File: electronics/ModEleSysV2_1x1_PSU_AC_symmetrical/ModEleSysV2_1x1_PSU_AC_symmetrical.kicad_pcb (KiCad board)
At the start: 2 copper layers, 43.2 x 49.5 mm, 30 parts, among them J2 Jack-DC, SW1 switch_DPDT, U1 LM317, U2 LM337

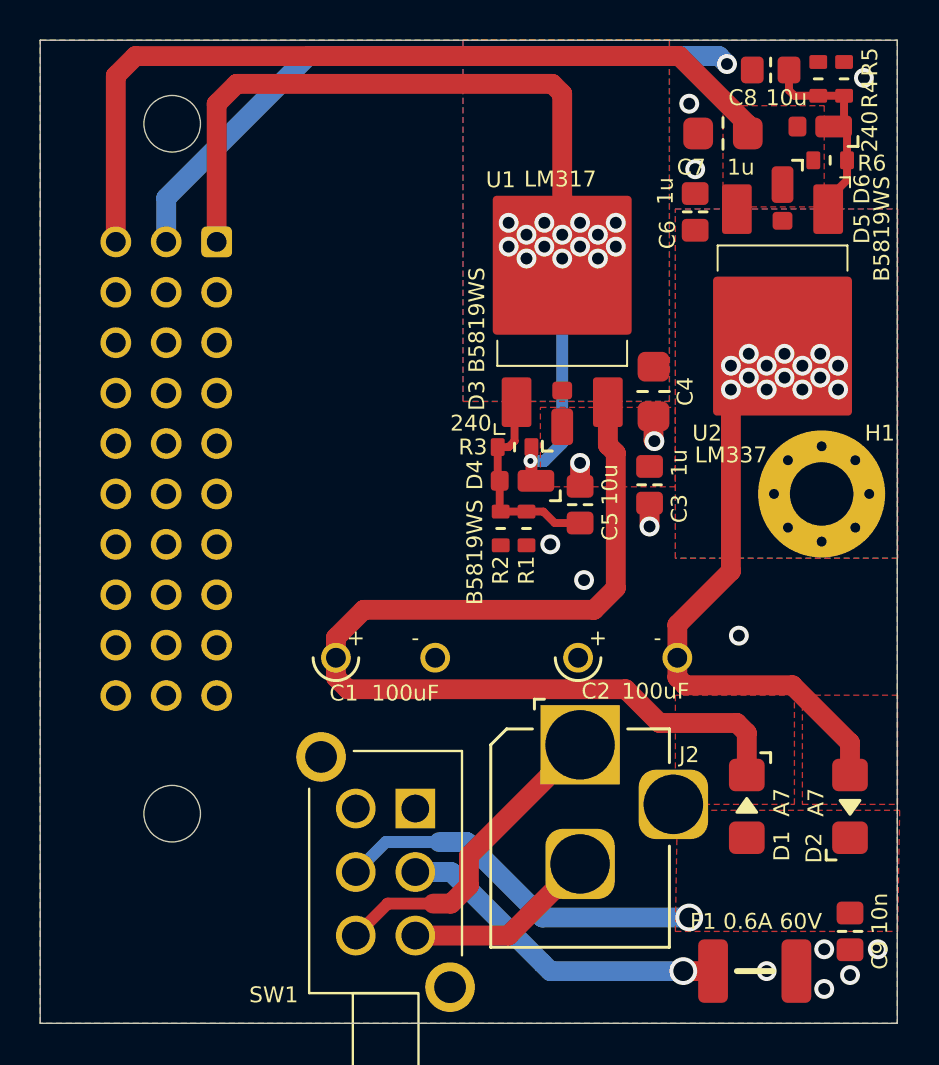
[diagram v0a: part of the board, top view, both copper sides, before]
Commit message: updated PCB with easier to place components and added more output capacitance
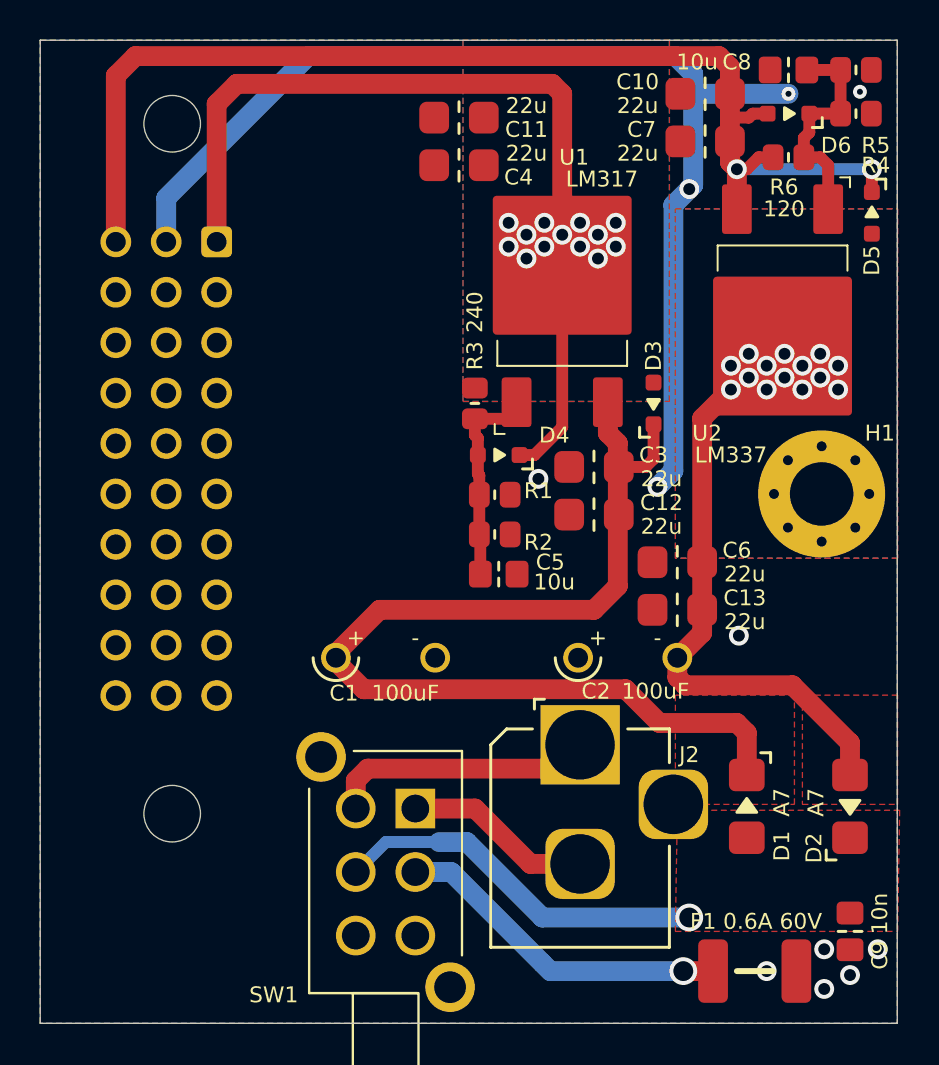
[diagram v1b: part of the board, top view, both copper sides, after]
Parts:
- added C10: 22u, SquantorCapacitor:C_1206_0805, F.Cu at (173.2, 66.2)
- added C11: 22u, SquantorCapacitor:C_1206_0805, F.Cu at (160.8, 67.4)
- added C12: 22u, SquantorCapacitor:C_1206_0805, F.Cu at (167.6, 87.4)
- added C13: 22u, SquantorCapacitor:C_1206_0805, F.Cu at (171.8, 92.2)
- C3, C6: value 1u -> 22u; footprint SquantorCapacitor:C_0805+0603 -> SquantorCapacitor:C_1206_0805
- C4, C7: value 1u -> 22u
- D3, D4, D5, D6: footprint SquantorDiodes:SOD-323HE-shikues -> SquantorDiodes:SOD-323-nexperia-hand
- R1, R2, R3, R4, R5: footprint SquantorResistor:R_0603_hand -> SquantorResistor:R_0805+0603
- R6: value 240 -> 120; footprint SquantorResistor:R_0603_hand -> SquantorResistor:R_0805+0603
- moved C6 17.7 mm to (171.8, 89.8), turned to 180 degrees
- moved C4 15.0 mm to (160.8, 69.8), turned to 180 degrees
- moved C5 5.39 mm to (162.8, 90.4), turned to 0 degrees
- moved D3 4.63 mm to (170.6, 81.8)
- moved D5 4.56 mm to (181.6, 72.2)
- moved R3 2.97 mm to (161.6, 81.8), turned to 90 degrees
- moved C3 2.94 mm to (167.6, 85.0), turned to 180 degrees
- moved R1 2.33 mm to (162.6, 86.4), turned to 0 degrees
- moved R6 2.11 mm to (177.4, 69.4)
- moved R5 1.95 mm to (180.8, 65.0), turned to 0 degrees
- moved R4 1.85 mm to (180.8, 67.2), turned to 0 degrees
- moved D4 1.77 mm to (162.8, 84.4)
- moved D6 1.73 mm to (177.4, 67.2)
- moved C7 0.98 mm to (173.2, 68.6)
- moved C8 0.90 mm to (177.4, 65.0)
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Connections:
- SW1 pad 1: unconnected-(SW1-SW1_P1-Pad1) -> /AC_NEUT_IN
- SW1 pad 3: /AC_NEUT_IN -> unconnected-(SW1-SW1_P2-Pad3)
- SW1 pad 4: /AC_PHASE1_IN -> unconnected-(SW1-SW2_P2-Pad4)
- SW1 pad 6: unconnected-(SW1-SW2_P2-Pad6) -> /AC_PHASE1_IN
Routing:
- net GND: track 37.2 -> 58.4 mm, vias 15 -> 11
- net /-aV: track 42.5 -> 59.3 mm, vias 0 -> 2
- net /DC1p: track 50.6 -> 53.5 mm
- net /AC_PHASE1_IN: track 16.2 -> 13.5 mm
- net /+aV: track 45.2 -> 43.0 mm, vias 15 -> 13
- net /-adj: track 10.3 -> 11.4 mm
- removed copper zone on F.Cu, net /-aV

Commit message: some more PCB modifications, changing output caps to larger values
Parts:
- removed C10, C11, C12, C13: 22u, SquantorCapacitor:C_1206_0805
- C4, C7: footprint SquantorCapacitor:C_1206_0805 -> SquantorCapacitor:C-025-065-elco
- moved C4 2.30 mm to (160.9, 67.5)
- moved C7 1.70 mm to (171.9, 67.5)
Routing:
- net /-aV: track 59.3 -> 60.7 mm
- net GND: track 58.4 -> 57.2 mm
- net /+aV: vias 13 -> 14

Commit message: preparations for production
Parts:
- N1: value 20240426 -> 20250323
- moved C7 0.45 mm to (171.4, 67.4)
- moved C4 0.06 mm to (160.9, 67.4)
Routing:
- net /-aV: track 60.7 -> 61.9 mm
- net /DC1n: track 27.5 -> 28.6 mm
- net /+aV: track 43.0 -> 42.5 mm

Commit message: reviewed and updated PCB's
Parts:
- removed SW1: switch_DPDT, SquantorSwitches:PS-22F02
- added J3: PINS_2X03, SquantorConnectors:DLL-XHY-6A, B.Cu at (47.5, 73.9)
- C1, C2: moved to B.Cu
- C4, C7: value 22u -> 47u
- U1, U2: footprint SquantorIC:TO-252_D-PAK_IRF -> SquantorIC:SOT-223
- moved C6 116.5 mm to (62.3, 49.9)
- moved R3 116.1 mm to (51.7, 44.3)
- moved U2 115.9 mm to (67.4, 41.4)
- moved C5 115.9 mm to (53.1, 52.9)
- moved D4 115.9 mm to (53.1, 46.9)
- moved C3 115.9 mm to (57.9, 47.5)
- moved D3 115.9 mm to (60.9, 44.3)
- moved R1 115.9 mm to (52.9, 48.9)
- moved R2 115.9 mm to (52.9, 50.9)
- moved D5 114.9 mm to (71.9, 38.1)
- moved D1 114.7 mm to (65.6, 68.6)
- moved J1 114.7 mm to (36.4, 51.6)
- moved R4 114.7 mm to (71.1, 33.7)
- moved R5 114.7 mm to (71.1, 31.5)
- moved C8 114.7 mm to (67.7, 31.5)
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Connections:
- J2 pad 1: /AC_PHASE1_IN -> /AC_NEUT_IN
- J2 pad 2: /AC_NEUT_IN -> /AC_PHASE1_IN
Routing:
- net /DC1p: track 53.5 -> 39.2 mm
- net /DC1n: track 28.6 -> 38.6 mm, vias 14 -> 10
- net /+aV: track 42.5 -> 32.5 mm, vias 14 -> 10
- net Net-(F1-Pad1): track 17.1 -> 24.3 mm
- net /AC_PHASE1_IN: track 13.5 -> 8.44 mm
- net /AC1_PHASE: track 19.0 -> 14.0 mm
- net /AC_NEUT_IN: track 9.46 -> 13.5 mm
- net GND: track 56.7 -> 52.8 mm, vias 11 -> 10

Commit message: Updated for production
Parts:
- N1: value 20250323 -> V:20260118
- moved D5 14.1 mm to (61.9, 28.1)
- moved D6 14.1 mm to (57.7, 23.7)
- moved H1 14.1 mm to (59.4, 42.9)
- moved J3 14.1 mm to (37.5, 63.9)
- moved U2 14.1 mm to (57.4, 31.4)
- moved C1 14.1 mm to (40.5, 49.8)
- moved C2 14.1 mm to (50.8, 49.8)
- moved C3 14.1 mm to (47.9, 37.5)
- moved C5 14.1 mm to (43.1, 42.9)
- moved C6 14.1 mm to (52.3, 39.9)
- moved C8 14.1 mm to (57.7, 21.5)
- moved C9 14.1 mm to (60.8, 64.9)
- moved D3 14.1 mm to (50.9, 34.3)
- moved D4 14.1 mm to (43.1, 36.9)
- moved F1 14.1 mm to (56.0, 66.9)
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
